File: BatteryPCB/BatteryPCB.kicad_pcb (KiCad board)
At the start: 2 copper layers, 68.6 x 53.3 mm, 22 parts, among them J1 Conn_01x01, J2 Conn_01x01, J3 Conn_01x01, J4 Conn_01x01_Socket, SW1 ANT11TFHQE, SW2 ANT11TFHQE, U1 LF50CV, U2 R05-100B, U3 R05-100B

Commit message: Updated from 3/30 comments
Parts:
- RV1, RV2: value 93PR5KLF -> CT-6EP502; footprint 93PR5KL:RES3_93_TTE -> Potentiometer_THT:Potentiometer_Bourns_3006P_Horizontal
- moved RV1 46.8 mm to (153.3, 84.8)
- moved J1 29.6 mm to (136.6, 94.9), turned to 90 degrees
- moved J2 24.0 mm to (140.6, 94.9), turned to 90 degrees
- moved J3 18.4 mm to (144.7, 94.9), turned to 90 degrees
- moved J4 7.62 mm to (161.0, 59.4)
- moved U2 5.08 mm to (112.7, 63.2)
- moved U3 5.08 mm to (133.0, 63.2)
- moved C4 5.07 mm to (125.4, 94.9)
- moved C3 4.49 mm to (124.4, 59.4)
- moved RV2 3.84 mm to (106.3, 86.9), turned to -90 degrees
- moved C5 3.59 mm to (153.3, 61.9)
- moved C6 2.98 mm to (153.3, 92.4), turned to -90 degrees
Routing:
- net HT: track 64.5 -> 29.7 mm
- net GND: track 32.8 -> 66.5 mm, vias 2 -> 0
- net -VSW: track 85.8 -> 57.0 mm
- net Net-(RV1-Pad1): track 49.4 -> 20.9 mm
- net Net-(RV1-Pad2): track 46.9 -> 24.4 mm
- net Net-(RV2-Pad2): track 27.0 -> 19.7 mm
- net Net-(C3-Pad2): track 50.7 -> 52.9 mm
- net Net-(RV2-Pad1): track 24.4 -> 23.0 mm
- added copper zone on B.Cu, net GND
- removed copper zone on F.Cu, net GND
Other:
- outline, holes or cut-outs redrawn
- board text added: "${REFERENCE}"

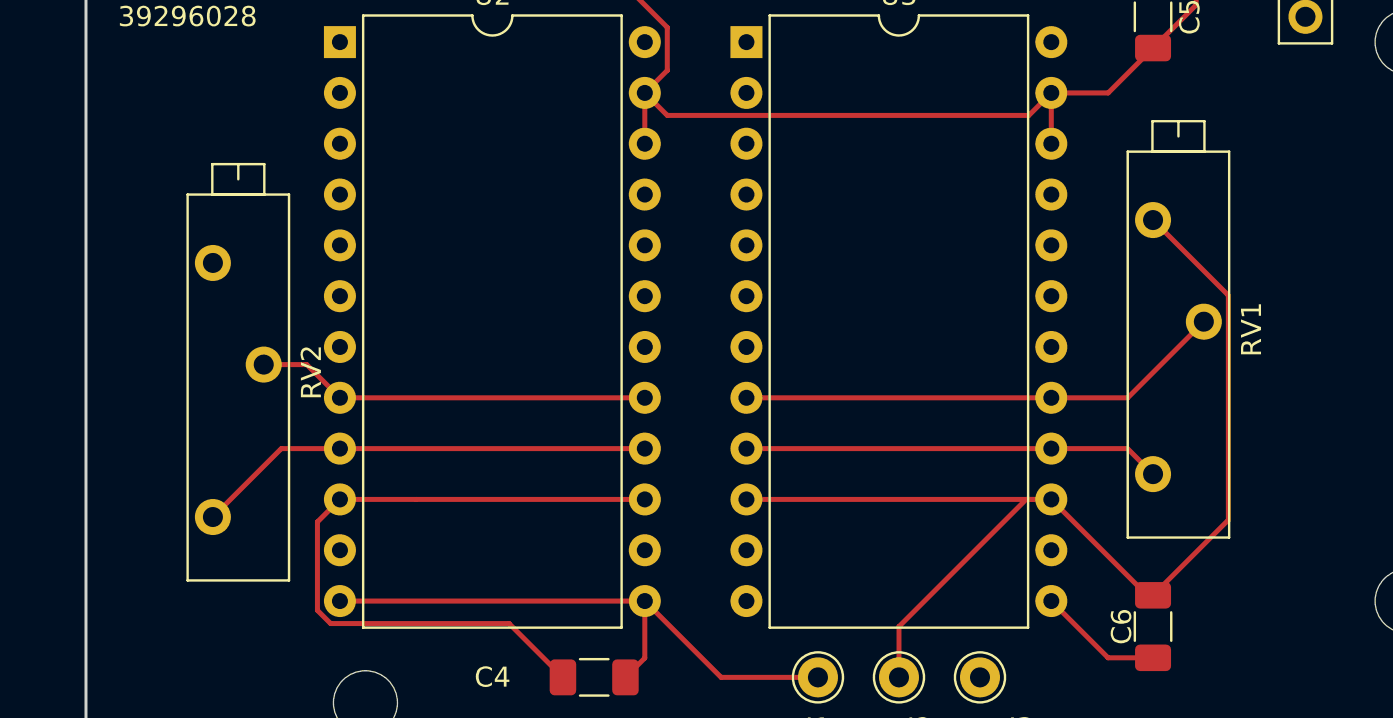
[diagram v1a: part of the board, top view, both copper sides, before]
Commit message: 4/1 trim pot change
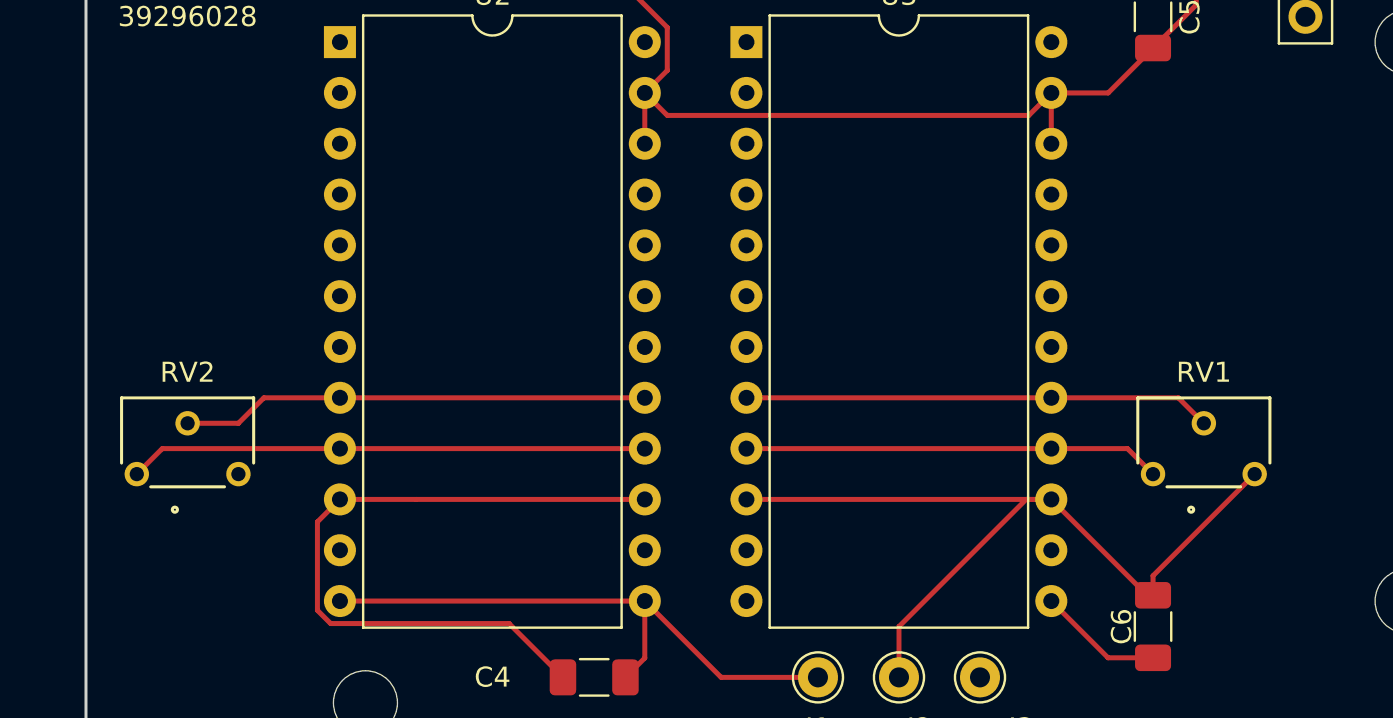
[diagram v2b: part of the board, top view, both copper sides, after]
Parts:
- RV1, RV2: value CT-6EP502 -> 64WR5KLF; footprint Potentiometer_THT:Potentiometer_Bourns_3006P_Horizontal -> 64WR5KLF:RES3_64W_TTE
- moved RV2 4.37 mm to (102.5, 84.8), turned to 0 degrees
- turned RV1 to 0 degrees
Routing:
- net -VSW: track 57.0 -> 43.3 mm
- net Net-(RV2-Pad2): track 19.7 -> 23.4 mm
- net Net-(RV2-Pad1): track 23.0 -> 25.9 mm
- net Net-(RV1-Pad2): track 24.4 -> 23.4 mm
